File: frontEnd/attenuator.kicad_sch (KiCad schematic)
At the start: 13 parts, among them U1 F1956NBGI

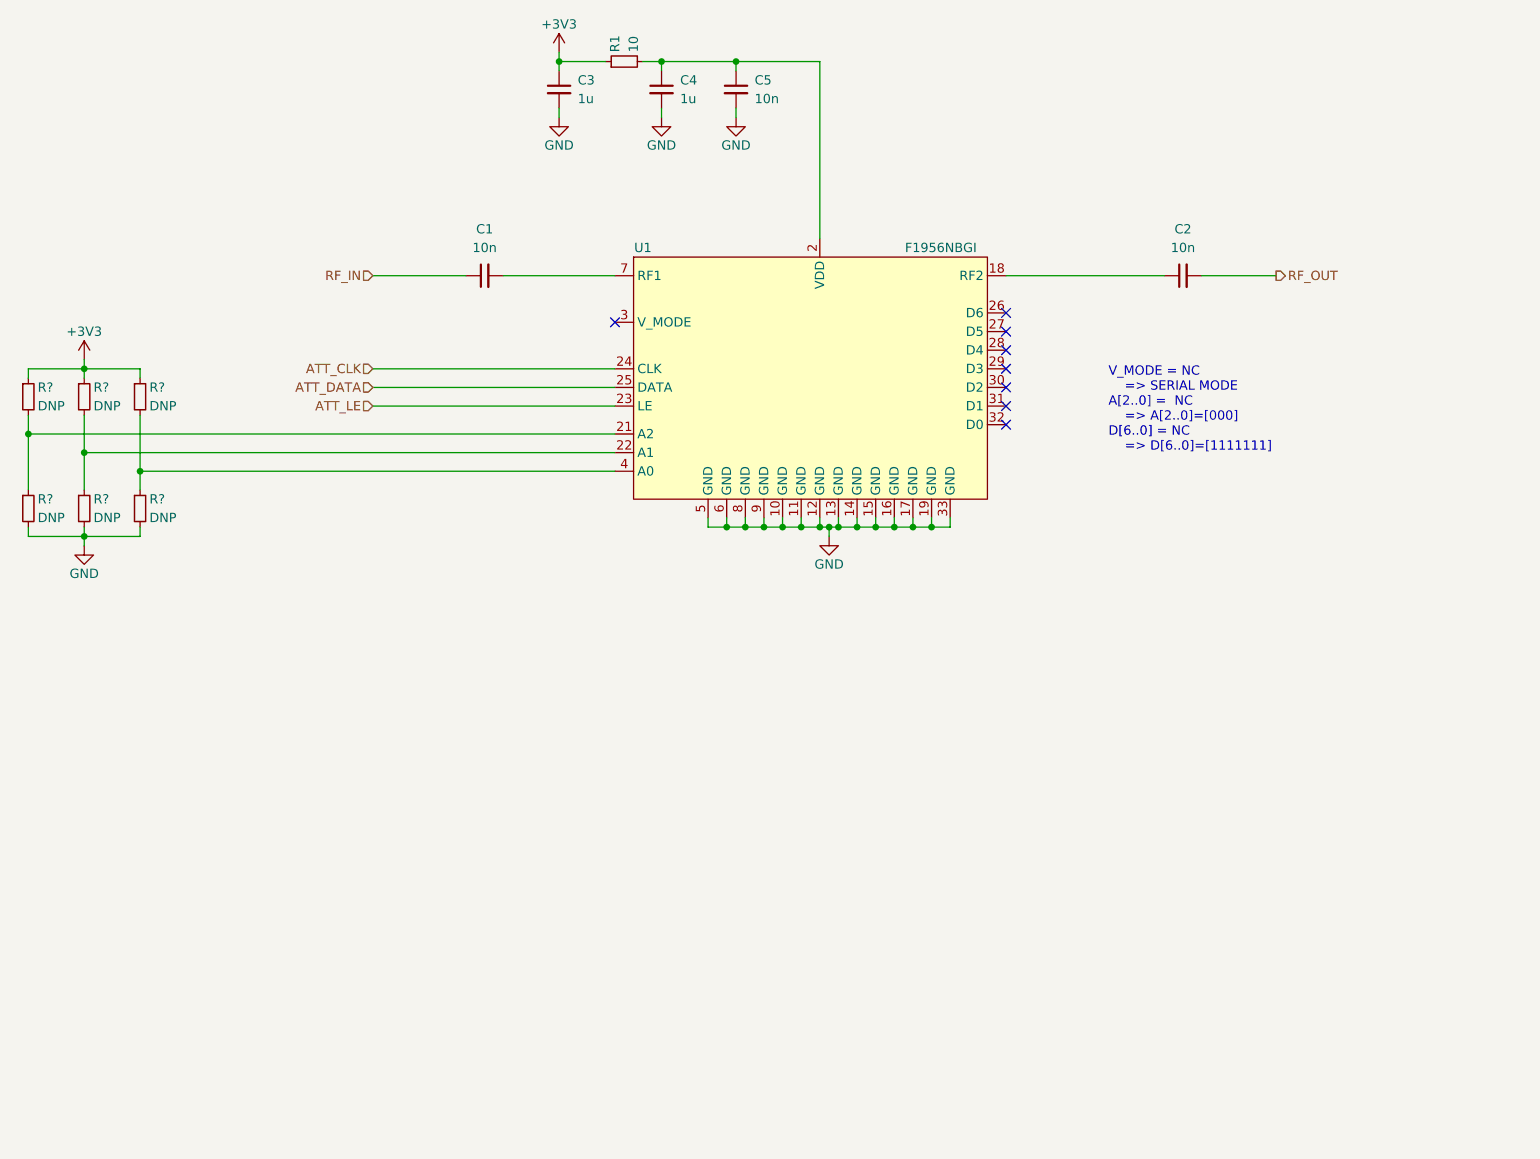
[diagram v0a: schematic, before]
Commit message: update schematics, add bypass for the attenuator
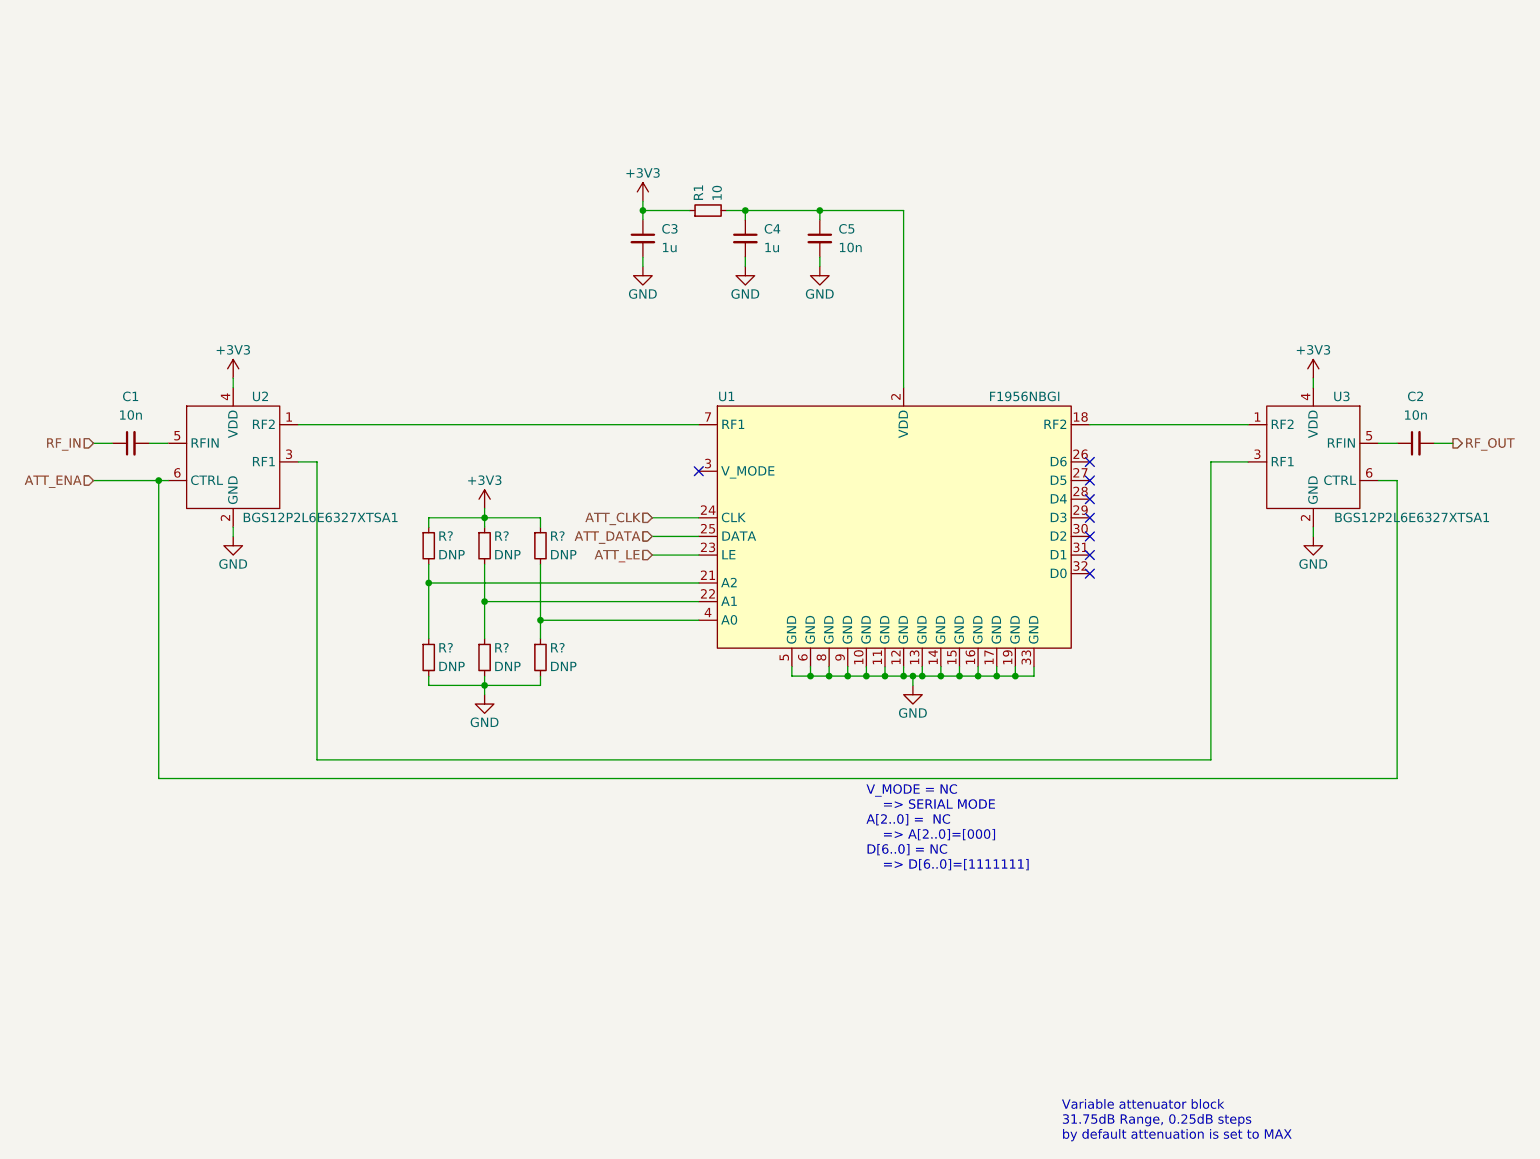
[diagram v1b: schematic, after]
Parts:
- added U2, U3: BGS12P2L6E6327XTSA1, symbol frontEnd:BGS12P2L6E6327XTSA1
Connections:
- net +3V3: now also U2.4 (VDD), U3.4 (VDD)
- net GND: now also U2.2 (GND), U3.2 (GND)
- net at C1.2: now also U2.5 (RFIN); no longer U1.7 (RF1)
- net at C2.1: now also U3.5 (RFIN); no longer U1.18 (RF2)
- new net: U1.18 (RF2), U3.1 (RF2)
- new net: U2.3 (RF1), U3.3 (RF1)
- new net: U1.7 (RF1), U2.1 (RF2)
- new net ATT_ENA: U2.6 (CTRL), U3.6 (CTRL)
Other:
- note added: "Variable attenuator block 31.75dB Range, 0.25dB steps by default attenuation is set to MAX"
- moved on the sheet: C1, C2, C3, C4, C5, R1, R?, U1
